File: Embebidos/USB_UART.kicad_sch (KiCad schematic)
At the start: 9 parts, among them J1 USB_A, Q1 BC847, Q2 BC847

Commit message: aa
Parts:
- renumbered Q1 to Q9
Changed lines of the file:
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@@
   (symbol (lib_id "Transistor_BJT:BC847") (at 196.85 90.17 0) (unit 1)
     (in_bom yes) (on_board yes) (fields_autoplaced)
-    (property "Reference" "Q1" (id 0) (at 201.93 88.8999 0)
+    (property "Reference" "Q9" (id 0) (at 201.93 88.8999 0)
       (effects (font (size 1.27 1.27)) (justify left))
     )

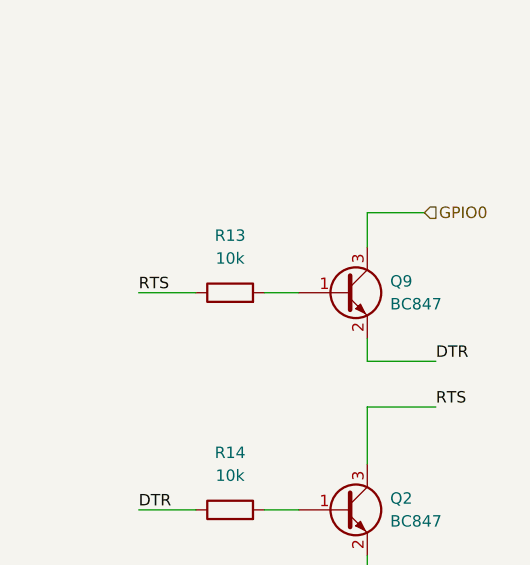
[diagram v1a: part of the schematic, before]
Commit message: fix:  track clearance cp2102x fixed
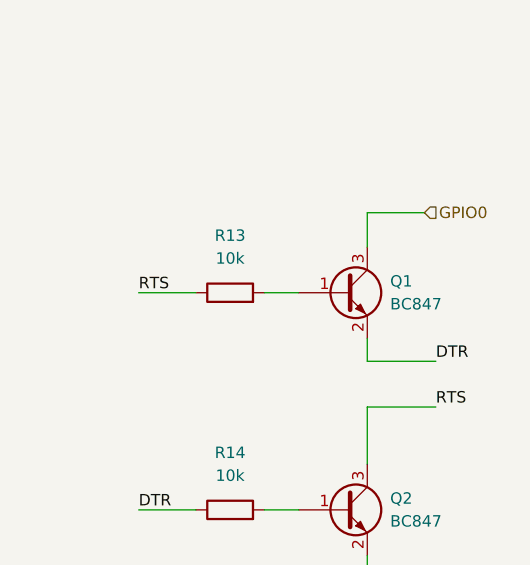
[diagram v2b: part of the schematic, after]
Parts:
- renumbered Q9 to Q1
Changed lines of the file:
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@@
   (symbol (lib_id "Transistor_BJT:BC847") (at 196.85 90.17 0) (unit 1)
     (in_bom yes) (on_board yes) (fields_autoplaced)
-    (property "Reference" "Q9" (id 0) (at 201.93 88.8999 0)
+    (property "Reference" "Q1" (id 0) (at 201.93 88.8999 0)
       (effects (font (size 1.27 1.27)) (justify left))
     )
